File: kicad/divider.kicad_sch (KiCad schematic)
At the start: 9 parts, among them J39 SPI, Q6 2N3904, Q8 2N3904, U11 ATtiny24A-P, U14 74LS241

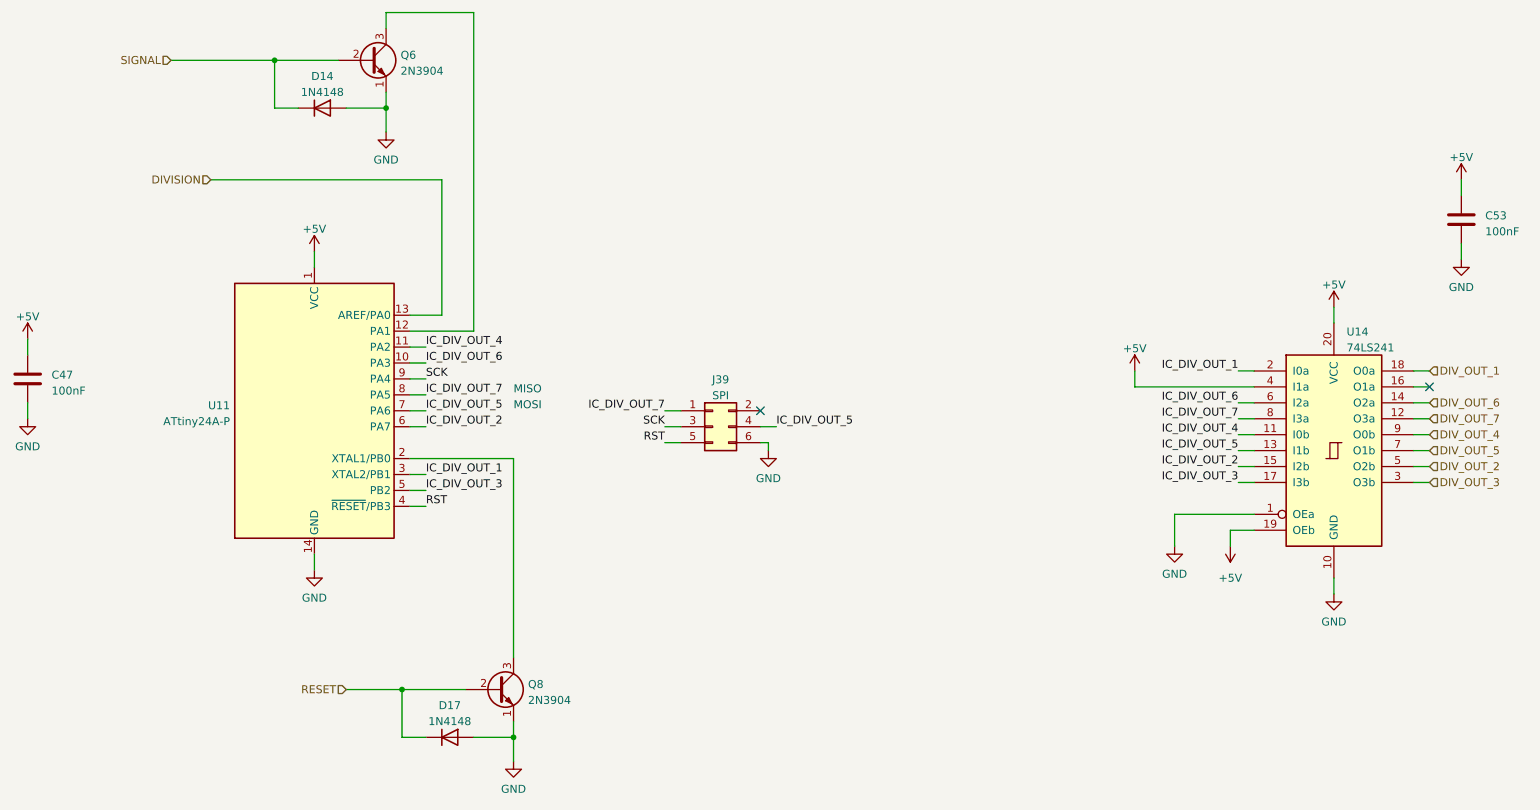
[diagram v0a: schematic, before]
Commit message: Updating board for new footprint libraries
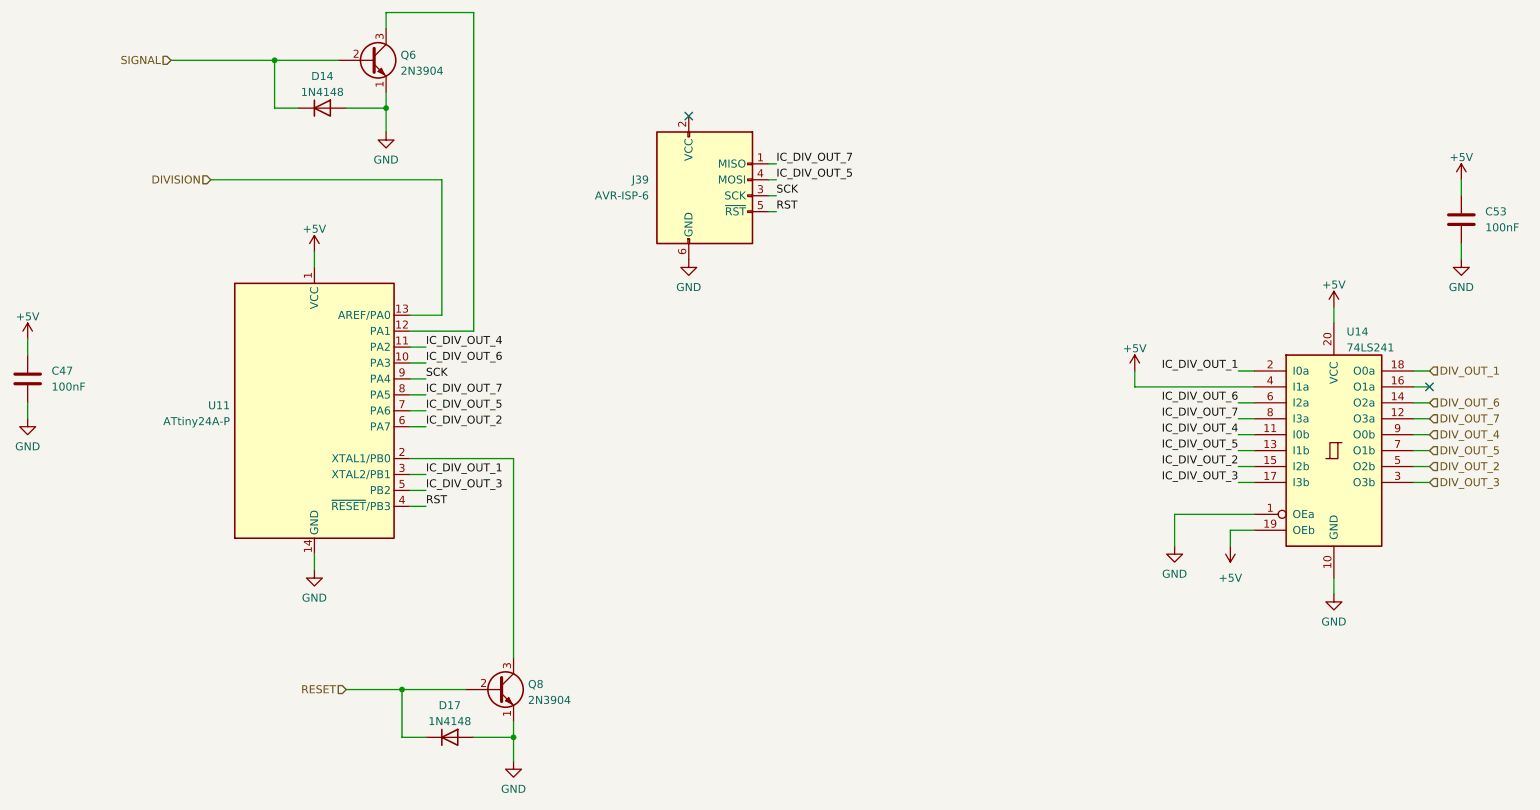
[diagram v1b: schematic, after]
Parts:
- removed J39: SPI, Connector_PinHeader_2.54mm:PinHeader_2x03_P2.54mm_Vertical, symbol Connector_Generic:Conn_02x03_Odd_Even
- added J39: AVR-ISP-6, Connector_PinHeader_2.54mm:PinHeader_2x03_P2.54mm_Vertical, symbol Connector:AVR-ISP-6
- C47, C53: symbol Rumblesan Standard Parts:C -> Rumblesan_Standard_Parts:C
- Q6, Q8: footprint Rumblesan_Standard_Parts:TO-92_Inline_Wide -> Package_TO_SOT_THT:TO-92_Inline_Wide
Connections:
- net GND: now also J39.6 (GND)
- net IC_DIV_OUT_5: now also J39.4 (MOSI)
- net IC_DIV_OUT_7: now also J39.1 (MISO)
- net RST: now also J39.5 (~{RST})
- net SCK: now also J39.3 (SCK)
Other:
- note removed: "MISO"
- note removed: "MOSI"

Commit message: Updating with rev03 changes
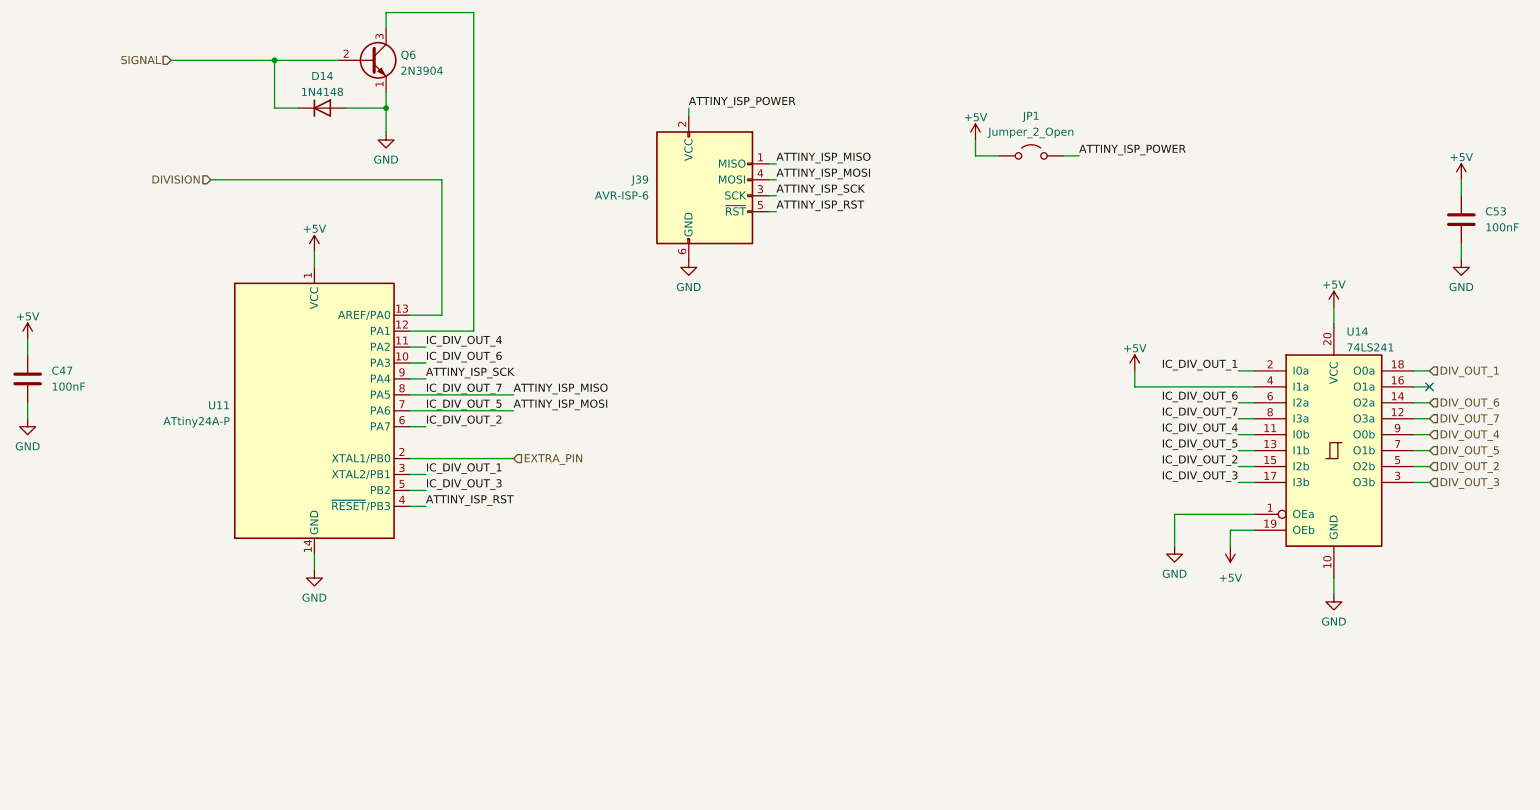
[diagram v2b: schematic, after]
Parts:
- removed D17: 1N4148, Rumblesan_Standard_Parts:D_DO-35_SOD27_P7.62mm_Horizontal, symbol Device:D
- removed Q8: 2N3904, Package_TO_SOT_THT:TO-92_Inline_Wide, symbol Transistor_BJT:2N3904
- added JP1: Jumper_2_Open, Connector_PinHeader_2.54mm:PinHeader_1x02_P2.54mm_Vertical, symbol Jumper:Jumper_2_Open
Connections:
- net +5V: now also JP1.1 (A)
- net ATTINY_ISP_POWER: now reaches J39.2 (VCC)
- net ATTINY_ISP_POWER: now also JP1.2 (B)
- net EXTRA_PIN: now reaches U11.2 (XTAL1/PB0)
- net IC_DIV_OUT_5 renamed ATTINY_ISP_MOSI
- net IC_DIV_OUT_7 renamed ATTINY_ISP_MISO
- net RST renamed ATTINY_ISP_RST
- net SCK renamed ATTINY_ISP_SCK
- no-connect marks 2 -> 1
